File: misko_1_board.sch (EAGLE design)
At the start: 147 parts, among them IC1 ATMEGA1281-16AU, IC10 ORG1510-MK4, IC11 TPS3808G33DBVT, IC12 LTC4425, IC13 RN4678_BT_MODULE, IC14 ADXL345, IC15 74HCT1G32, IC16 FM25W256-SOIC, IC17 MICROSD_SPI_MODE, IC18 FH12-30S-0.5SH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

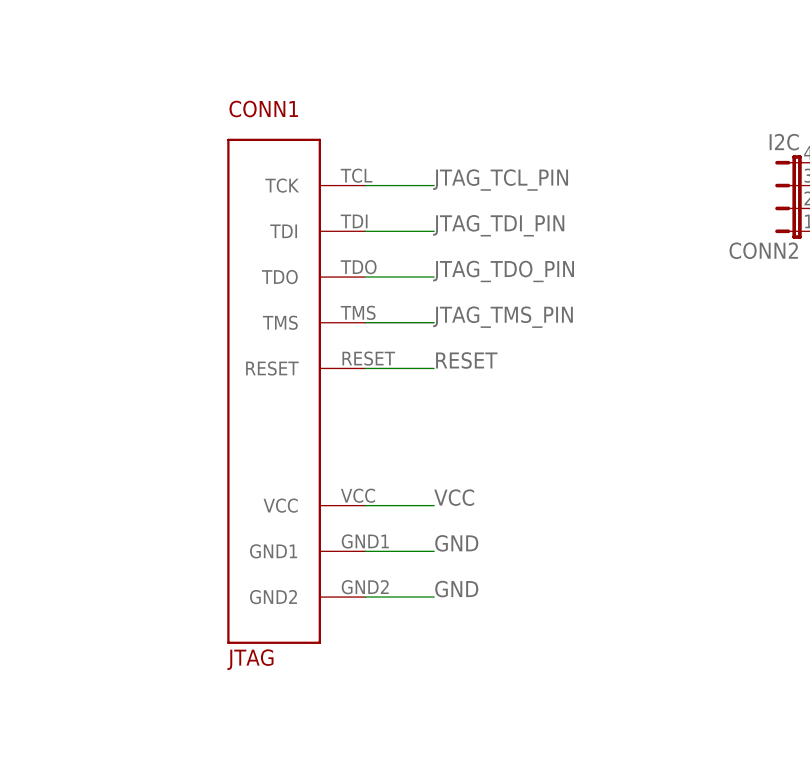
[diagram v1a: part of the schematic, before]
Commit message: - corrected JTAG 1.27mm 10pin header.lbr; pinout was pairwise swapped - corrected board layout to accommodate new JTAG header orientation
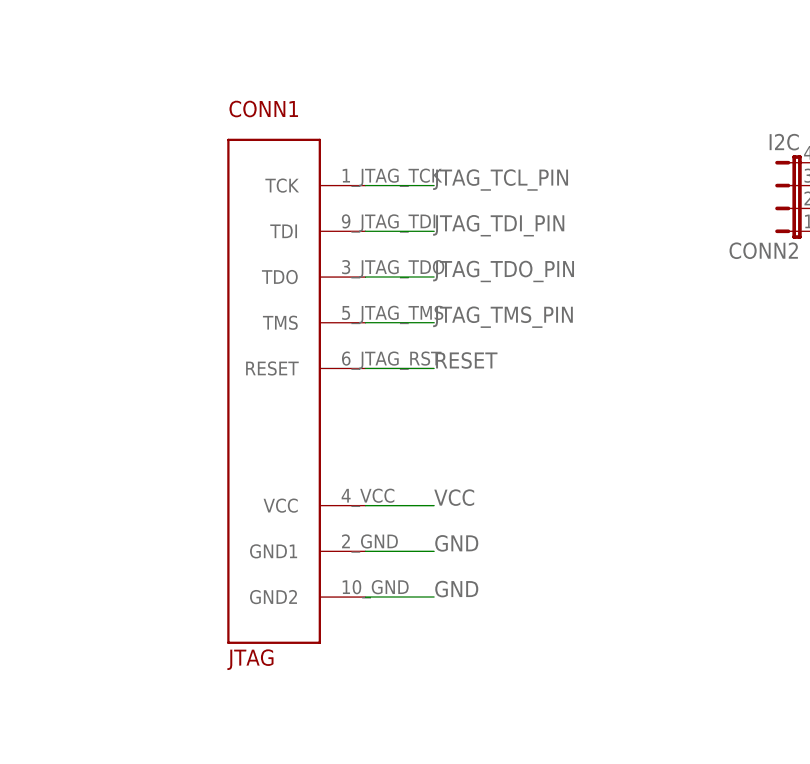
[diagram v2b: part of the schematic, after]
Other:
- moved on the sheet: CONN1
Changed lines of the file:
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@@
 <?xml version="1.0" encoding="utf-8"?>
 <!DOCTYPE eagle SYSTEM "eagle.dtd">
-<eagle version="8.3.1">
+<eagle version="8.3.2">
 <drawing>
 <settings>

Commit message: - added zener protection diodes to wifi, bluetooth modules and 5v0 input
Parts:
- added D4: BZT52C3V3-E3-08, zener:ZENERSOD123
- added D5: BZT52C4V3-E3-18, zener:ZENERSOD123
- added D6: 1N4733AW-TP, zener:ZENERSOD123
- D3: value MMSZ5231B-DIO -> BZT52C5V1-E3-18; device diode:DIODE-SOD123 -> zener:ZENERSOD123
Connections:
- net 5V0: now also D6.C
- net GND: now also D4.A, D5.A, D6.A
- net VCC: now also D4.C
- net V_LIION+: now also D5.C
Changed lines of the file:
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@@
 <part name="R28" library="resistor" library_urn="urn:adsk.eagle:library:348" deviceset="R-EU_" device="R0805" value="10k"/>
 <part name="C26" library="rcl" deviceset="C-EU" device="C0805" value="33pF"/>
-<part name="D3" library="diode" library_urn="urn:adsk.eagle:library:210" deviceset="DIODE-" device="SOD123" value="MMSZ5231B-DIO"/>
+<part name="D3" library="zener" library_urn="urn:adsk.eagle:library:449000" deviceset="ZENER" device="SOD123" package3d_urn="urn:adsk.eagle:package:449003/1" value="BZT52C5V1-E3-18"/>
 <part name="IC20" library="ATWINC1500-MR210PB WiFi Module" deviceset="ATWINC1500-MR210PB" device=""/>
 <part name="R21" library="rcl" deviceset="R-EU_" device="R0805" value="1M"/>
@@
 <part name="TP11" library="testpad" deviceset="PTR1" device="TP14R" value="Bluetooth Wakeup Pin"/>
 <part name="C45" library="rcl" deviceset="C-EU" device="C0805" value="0.1µF"/>
+<part name="D5" library="zener" library_urn="urn:adsk.eagle:library:449000" deviceset="ZENER" device="SOD123" package3d_urn="urn:adsk.eagle:package:449003/1" value="BZT52C4V3-E3-18"/>
+<part name="D4" library="zener" library_urn="urn:adsk.eagle:library:449000" deviceset="ZENER" device="SOD123" package3d_urn="urn:adsk.eagle:package:449003/1" value="BZT52C3V3-E3-08"/>
+<part name="D6" library="zener" library_urn="urn:adsk.eagle:library:449000" deviceset="ZENER" device="SOD123" package3d_urn="urn:adsk.eagle:package:449003/1" value="1N4733AW-TP"/>
 </parts>
 <sheets>
@@
 <instance part="R28" gate="G$1" x="190.5" y="314.96"/>
 <instance part="C26" gate="G$1" x="264.16" y="-533.4" rot="R180"/>
-<instance part="D3" gate="G$1" x="271.78" y="-533.4" rot="R90"/>
+<instance part="D3" gate="G$1" x="271.78" y="-533.4" smashed="yes" rot="R90">
+<attribute name="NAME" x="270.002" y="-535.94" size="1.778" layer="95" rot="R90"/>
+<attribute name="VALUE" x="274.32" y="-532.003" size="1.778" layer="96"/>
+</instance>
 <instance part="IC20" gate="G$1" x="78.74" y="-370.84"/>
 <instance part="R21" gate="G$1" x="165.1" y="-353.06" rot="R180"/>
@@
 <instance part="TP11" gate="G$1" x="266.67" y="753.19" rot="R270"/>
 <instance part="C45" gate="G$1" x="50.8" y="502.92" rot="R270"/>
+<instance part="D5" gate="G$1" x="104.14" y="-350.52" smashed="yes" rot="R270">
+<attribute name="NAME" x="105.918" y="-347.98" size="1.778" layer="95" rot="R270"/>
+<attribute name="VALUE" x="100.203" y="-350.52" size="1.778" layer="96" rot="R90"/>
+</instance>
+<instance part="D4" gate="G$1" x="162.56" y="-12.7" smashed="yes" rot="R270">
+<attribute name="NAME" x="164.338" y="-10.16" size="1.778" layer="95" rot="R270"/>
+<attribute name="VALUE" x="167.64" y="-11.303" size="1.778" layer="96"/>
+</instance>
+<instance part="D6" gate="G$1" x="332.74" y="213.36" smashed="yes" rot="R90">
+<attribute name="NAME" x="330.962" y="210.82" size="1.778" layer="95" rot="R90"/>
+<attribute name="VALUE" x="335.28" y="212.217" size="1.778" layer="96"/>
+</instance>
 </instances>
 <busses>
@@
 <label x="165.1" y="-15.24" size="1.778" layer="95"/>
 <pinref part="C29" gate="G$1" pin="1"/>
-<wire x1="154.94" y1="-15.24" x2="165.1" y2="-15.24" width="0.1524" layer="91"/>
+<wire x1="154.94" y1="-15.24" x2="162.56" y2="-15.24" width="0.1524" layer="91"/>
 <junction x="154.94" y="-15.24"/>
+<pinref part="D4" gate="G$1" pin="C"/>
+<wire x1="162.56" y1="-15.24" x2="165.1" y2="-15.24" width="0.1524" layer="91"/>
+<junction x="162.56" y="-15.24"/>
 </segment>
 </net>
@@
 <segment>
 <pinref part="IC20" gate="G$1" pin="GND"/>
-<wire x1="81.28" y1="-350.52" x2="96.52" y2="-350.52" width="0.1524" layer="91"/>
-<label x="96.52" y="-350.52" size="1.778" layer="95"/>
+<wire x1="81.28" y1="-350.52" x2="88.9" y2="-350.52" width="0.1524" layer="91"/>
+<label x="88.9" y="-350.52" size="1.778" layer="95"/>
 </segment>
 <segment>
@@
 <segment>
 <pinref part="C29" gate="G$1" pin="2"/>
-<wire x1="154.94" y1="-7.62" x2="165.1" y2="-7.62" width="0.1524" layer="91"/>
-<label x="165.1" y="-7.62" size="1.778" layer="95"/>
+<wire x1="154.94" y1="-7.62" x2="154.94" y2="-2.54" width="0.1524" layer="91"/>
+<label x="154.94" y="-2.54" size="1.778" layer="95"/>
 </segment>
 <segment>
@@
 <label x="25.4" y="502.92" size="1.778" layer="95"/>
 </segment>
+<segment>
+<pinref part="D5" gate="G$1" pin="A"/>
+<wire x1="104.14" y1="-347.98" x2="104.14" y2="-340.36" width="0.1524" layer="91"/>
+<label x="104.14" y="-340.36" size="1.778" layer="95"/>
+</segment>
+<segment>
+<pinref part="D4" gate="G$1" pin="A"/>
+<wire x1="162.56" y1="-10.16" x2="162.56" y2="-2.54" width="0.1524" layer="91"/>
+<label x="162.56" y="-2.54" size="1.778" layer="95"/>
+</segment>
+<segment>
+<pinref part="D6" gate="G$1" pin="A"/>
+<wire x1="332.74" y1="210.82" x2="332.74" y2="205.74" width="0.1524" layer="91"/>
+<label x="332.74" y="205.74" size="1.778" layer="95"/>
+</segment>
 </net>
 <net name="5V0" class="1">
@@
 <wire x1="332.74" y1="226.06" x2="332.74" y2="220.98" width="0.1524" layer="91"/>
 <junction x="332.74" y="220.98"/>
+<pinref part="D6" gate="G$1" pin="C"/>
+<wire x1="332.74" y1="215.9" x2="332.74" y2="220.98" width="0.1524" layer="91"/>
 </segment>
 <segment>
@@
 <segment>
 <pinref part="IC20" gate="G$1" pin="VBATT"/>
-<wire x1="81.28" y1="-353.06" x2="96.52" y2="-353.06" width="0.1524" layer="91"/>
-<label x="96.52" y="-353.06" size="1.778" layer="95"/>
+<wire x1="81.28" y1="-353.06" x2="104.14" y2="-353.06" width="0.1524" layer="91"/>
+<label x="109.22" y="-353.06" size="1.778" layer="95"/>
+<pinref part="D5" gate="G$1" pin="C"/>
+<wire x1="104.14" y1="-353.06" x2="109.22" y2="-353.06" width="0.1524" layer="91"/>
+<junction x="104.14" y="-353.06"/>
 </segment>
 </net>
@@
 <segment>
 <pinref part="IC13" gate="G$1" pin="LDO33_O"/>
-<wire x1="134.62" y1="-25.4" x2="154.94" y2="-25.4" width="0.1524" layer="91"/>
+<wire x1="134.62" y1="-25.4" x2="147.32" y2="-25.4" width="0.1524" layer="91"/>
 <label x="154.94" y="-17.78" size="1.778" layer="95"/>
 <pinref part="IC13" gate="G$1" pin="VDD_IO"/>
-<wire x1="134.62" y1="-17.78" x2="154.94" y2="-17.78" width="0.1524" layer="91"/>
-<wire x1="154.94" y1="-17.78" x2="154.94" y2="-25.4" width="0.1524" layer="91"/>
+<wire x1="134.62" y1="-17.78" x2="147.32" y2="-17.78" width="0.1524" layer="91"/>
+<wire x1="147.32" y1="-17.78" x2="147.32" y2="-25.4" width="0.1524" layer="91"/>
 </segment>
 </net>
@@
 with this version.
 </note>
+<note version="8.3" severity="warning">
+Since Version 8.3, EAGLE supports URNs for individual library
+assets (packages, symbols, and devices). The URNs of those assets
+will not be understood (or retained) with this version.
+</note>
+<note version="8.3" severity="warning">
+Since Version 8.3, EAGLE supports the association of 3D packages
+with devices in libraries, schematics, and board files. Those 3D
+packages will not be understood (or retained) with this version.
+</note>
 </compatibility>

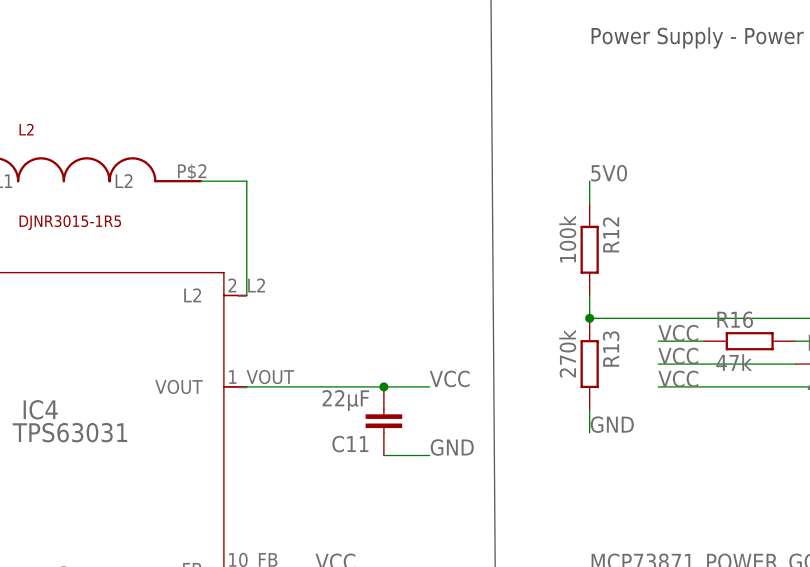
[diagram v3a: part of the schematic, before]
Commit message: - added 3V3 zener protection diode
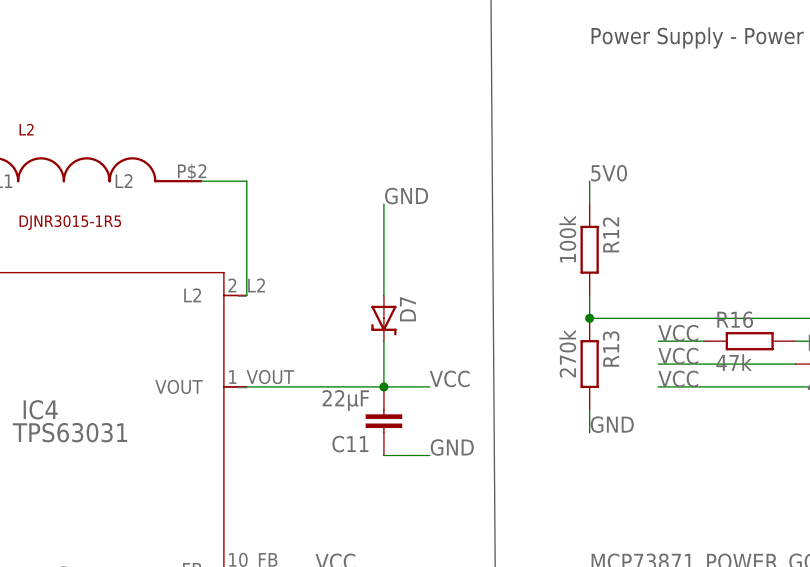
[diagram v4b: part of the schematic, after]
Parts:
- added D7: (no value), zener:ZENER
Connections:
- net 5V0: now also D6.CAT; no longer D6.C
- net GND: now also D3.AN, D4.AN, D5.AN, D6.AN, D7.AN; no longer D3.A, D4.A, D5.A, D6.A
- net VCC: now also D4.CAT, D7.CAT; no longer D4.C
- net V_LIION+: now also D3.CAT, D5.CAT; no longer D3.C, D5.C

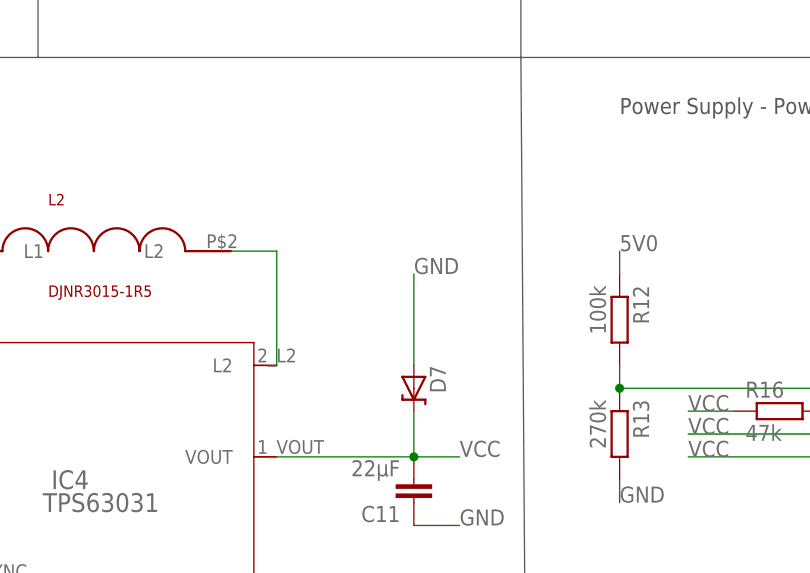
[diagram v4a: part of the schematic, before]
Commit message: - specified value for 3V3 protection diode (is in reality a 3V8 diode)
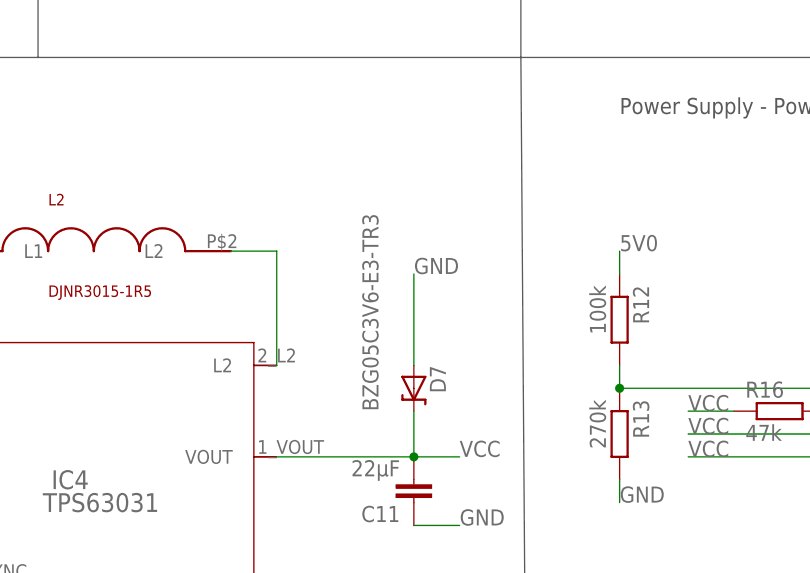
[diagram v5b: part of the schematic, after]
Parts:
- D7: value (none) -> BZG05C3V6-E3-TR3
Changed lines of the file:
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@@
 <part name="D4" library="zener" library_urn="urn:adsk.eagle:library:449000" deviceset="ZENER" device="SOD123" package3d_urn="urn:adsk.eagle:package:449003/1" value="BZT52C3V3-E3-08"/>
 <part name="D6" library="zener" library_urn="urn:adsk.eagle:library:449000" deviceset="ZENER" device="SOD123" package3d_urn="urn:adsk.eagle:package:449003/1" value="1N4733AW-TP"/>
-<part name="D7" library="zener" library_urn="urn:adsk.eagle:library:449000" deviceset="ZENER" device=""/>
+<part name="D7" library="zener" library_urn="urn:adsk.eagle:library:449000" deviceset="ZENER" device="" value="BZG05C3V6-E3-TR3"/>
 </parts>
 <sheets>
@@
 <attribute name="VALUE" x="335.28" y="212.217" size="1.778" layer="96"/>
 </instance>
-<instance part="D7" gate="G$1" x="111.76" y="523.24" rot="R270"/>
+<instance part="D7" gate="G$1" x="111.76" y="523.24" smashed="yes" rot="R270">
+<attribute name="NAME" x="113.538" y="525.78" size="1.778" layer="95" rot="R270"/>
+<attribute name="VALUE" x="107.823" y="520.7" size="1.778" layer="96" rot="R90"/>
+</instance>
 </instances>
 <busses>
